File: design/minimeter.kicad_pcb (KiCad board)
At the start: 2 copper layers, 44.4 x 26.7 mm, 15 parts, among them J1 Conn_01x02_Pin, J2 I2C, SW1 SW_Push_Dual, SW2 SW_Push_Dual

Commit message: Implement negative voltage measurement
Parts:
- R2: value 10K -> 4.7K
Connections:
- net /PULL_10K renamed /PULL_4.7K
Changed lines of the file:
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@@
 	(net 11 "unconnected-(A1-RESET-PadRST2)")
 	(net 12 "/BTN_SEL")
-	(net 13 "/PULL_10K")
+	(net 13 "/PULL_4.7K")
 	(net 14 "unconnected-(A1-3.3V-Pad3V3)")
 	(net 15 "unconnected-(A1-PadD6)")
@@
 			)
 		)
-		(property "Value" "10K"
+		(property "Value" "4.7K"
 			(at 3.81 -2.37 0)
 			(layer "B.Fab")
@@
 			(layers "*.Cu" "*.Mask")
 			(remove_unused_layers no)
-			(net 13 "/PULL_10K")
+			(net 13 "/PULL_4.7K")
 			(pintype "passive")
 		)
@@
 			(layers "*.Cu" "*.Mask")
 			(remove_unused_layers no)
-			(net 13 "/PULL_10K")
+			(net 13 "/PULL_4.7K")
 			(pinfunction "D9")
 			(pintype "bidirectional")

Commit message: Update hardware to v3
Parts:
- removed R5: 220, Resistor_THT:R_Axial_DIN0207_L6.3mm_D2.5mm_P7.62mm_Horizontal
- C1: footprint Capacitor_THT:C_Rect_L7.0mm_W2.0mm_P5.00mm -> Capacitor_THT:C_Disc_D3.4mm_W2.1mm_P2.50mm
- R4: value 220 -> 100
- moved R2 1.27 mm to (57.1, 53.3)
- moved R3 1.27 mm to (57.1, 55.9)
- moved R4 1.27 mm to (57.1, 58.4)
- moved C1 0.64 mm to (73.7, 57.8)
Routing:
- net /IN_PROT: track 20.3 -> 26.5 mm
- net Net-(C1-Pad2): track 4.27 -> 6.01 mm
- net /PULL_1K: track 12.3 -> 11.0 mm
- net /PULL_110: track 8.67 -> 7.40 mm
- net /PULL_4.7K: track 15.9 -> 14.6 mm
- net /SPKR: track 15.0 -> 15.9 mm
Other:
- board text added: "MiniMeter v3 2026-01-28 Jasmine Tai"
- board text removed: "MiniMeter v2 2026-01-21 Jasmine Tai"

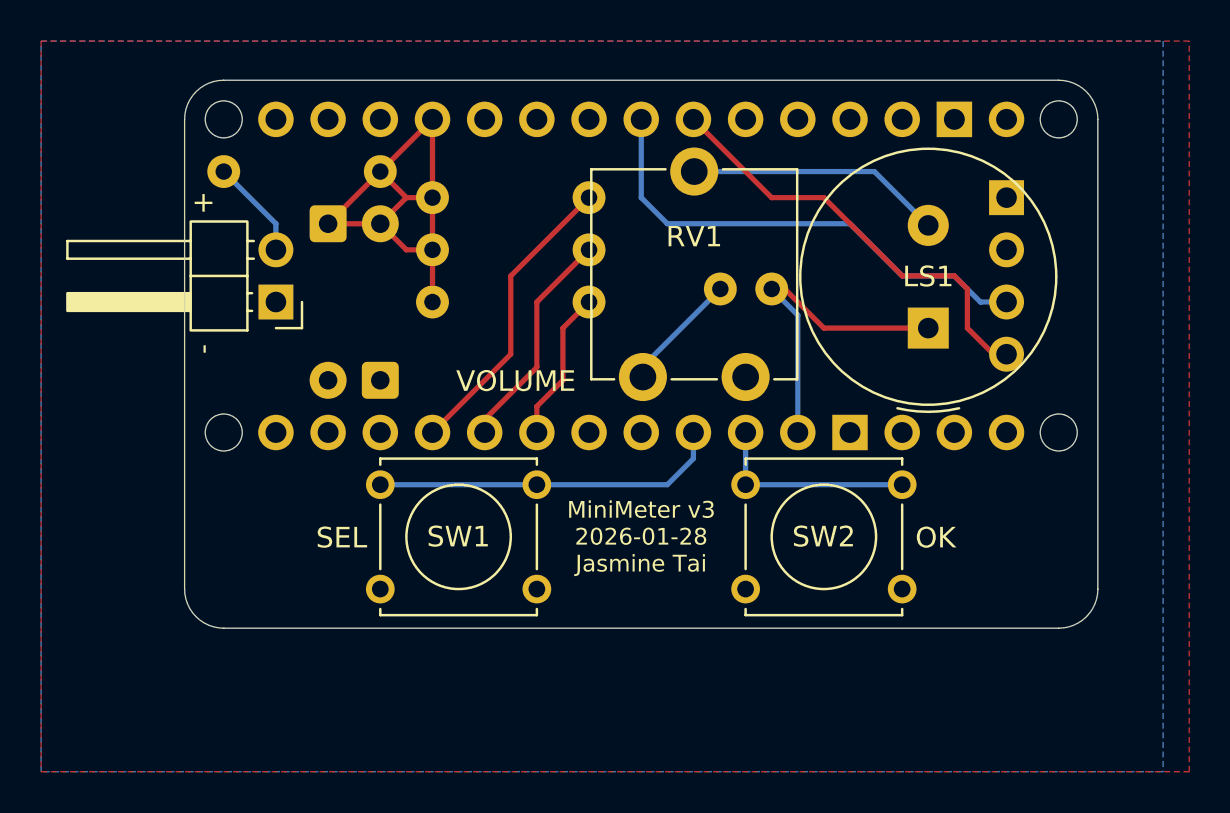
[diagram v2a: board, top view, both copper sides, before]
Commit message: Update footprints
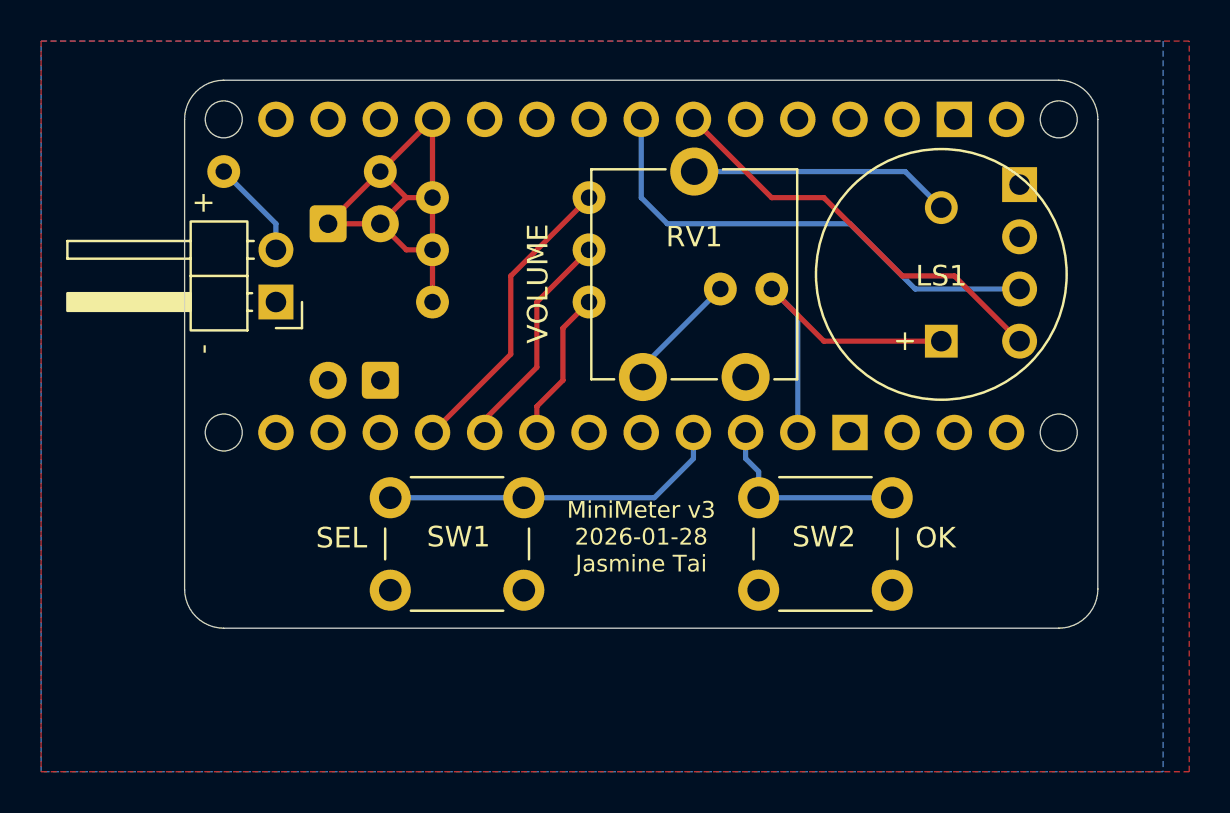
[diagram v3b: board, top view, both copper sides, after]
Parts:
- LS1: footprint Buzzer_Beeper:Buzzer_TDK_PS1240P02BT_D12.2mm_H6.5mm -> Buzzer_Beeper:MagneticBuzzer_ProSignal_ABT-410-RC
- SW1, SW2: footprint Button_Switch_THT:SW_Tactile_Straight_KSA0Axx1LFTR -> Button_Switch_THT:SW_PUSH_6mm
- moved LS1 0.90 mm to (81.9, 60.3)
- moved J2 0.90 mm to (85.7, 52.7)
- moved SW2 0.90 mm to (73.0, 67.9)
- moved SW1 0.80 mm to (55.1, 67.9)
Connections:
- net /PULL_110 renamed /PULL_100
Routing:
- net /SPKR: track 15.9 -> 16.8 mm
- net /SCL: track 21.1 -> 20.3 mm

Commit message: Update design to v4
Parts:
- added D3: LED_Filled, LED_THT:LED_D3.0mm, F.Cu at (49.5, 57.1)
- added R5: 820, Resistor_THT:R_Axial_DIN0207_L6.3mm_D2.5mm_P7.62mm_Horizontal, B.Cu at (47.0, 59.7)
- A1: footprint arduino-library:Arduino_Nano_Socket -> Module:Arduino_Nano_WithMountingHoles
- RV1: footprint Potentiometer_THT:Potentiometer_ACP_CA9-V10_Vertical -> Potentiometer_THT:Potentiometer_Bourns_3386F_Vertical
- moved A1 40.1 mm to (85.1, 64.8)
- moved D1 18.8 mm to (70.5, 52.1), turned to 180 degrees
- moved R1 11.4 mm to (52.1, 62.2), turned to 90 degrees
- moved J1 10.3 mm to (50.8, 68.6), turned to -90 degrees
- moved C1 4.62 mm to (74.9, 62.2)
- moved R4 4.58 mm to (59.7, 54.6), turned to -90 degrees
- moved SW1 3.90 mm to (59.0, 67.6)
- moved RV1 3.90 mm to (69.2, 59.8)
- moved R2 2.84 mm to (54.6, 54.6), turned to -90 degrees
- moved SW2 2.64 mm to (70.4, 67.6)
- moved D2 2.54 mm to (52.1, 52.1), turned to 0 degrees
- moved LS1 1.91 mm to (80.0, 60.3)
- moved R3 1.27 mm to (57.1, 54.6), turned to -90 degrees
- moved J2 0.90 mm to (85.1, 52.1)
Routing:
- net /IN_PROT: track 26.5 -> 0.00 mm
- net /PULL_4.7K: track 14.6 -> 3.59 mm
- net /SCL: track 20.3 -> 30.7 mm
- net /SPKR: track 16.8 -> 8.44 mm
- net /PULL_1K: track 11.0 -> 3.59 mm
- net Net-(D3-K): track 0.00 -> 6.13 mm
- net /LED: track 0.00 -> 5.08 mm
- net /BTN_SEL: track 16.8 -> 12.0 mm
- net /IN: track 4.86 -> 8.73 mm
- net /PULL_100: track 7.40 -> 3.59 mm
- net Net-(C1-Pad2): track 6.01 -> 9.28 mm
- net /SDA: track 24.1 -> 22.4 mm
- net Net-(LS1--): track 12.8 -> 13.7 mm
- added copper zone on B.Cu, net /IN_PROT
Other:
- board text added: "MiniMeter v4 2026.02.03 Jasmine Tai"
- board text removed: "MiniMeter v3 2026-01-28 Jasmine Tai"
- board text removed: "USB SIDE"

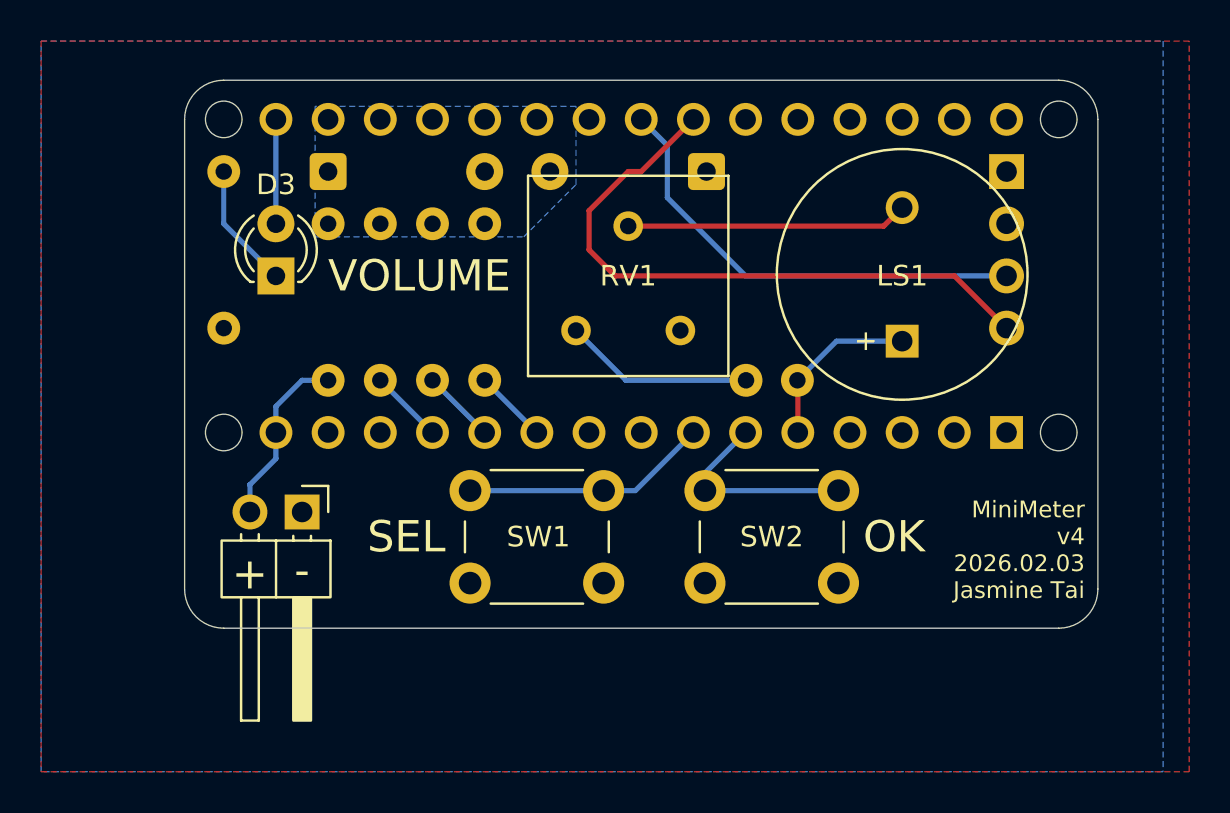
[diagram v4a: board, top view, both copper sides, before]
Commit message: Update PCB to v5 with updated trimpot footprint
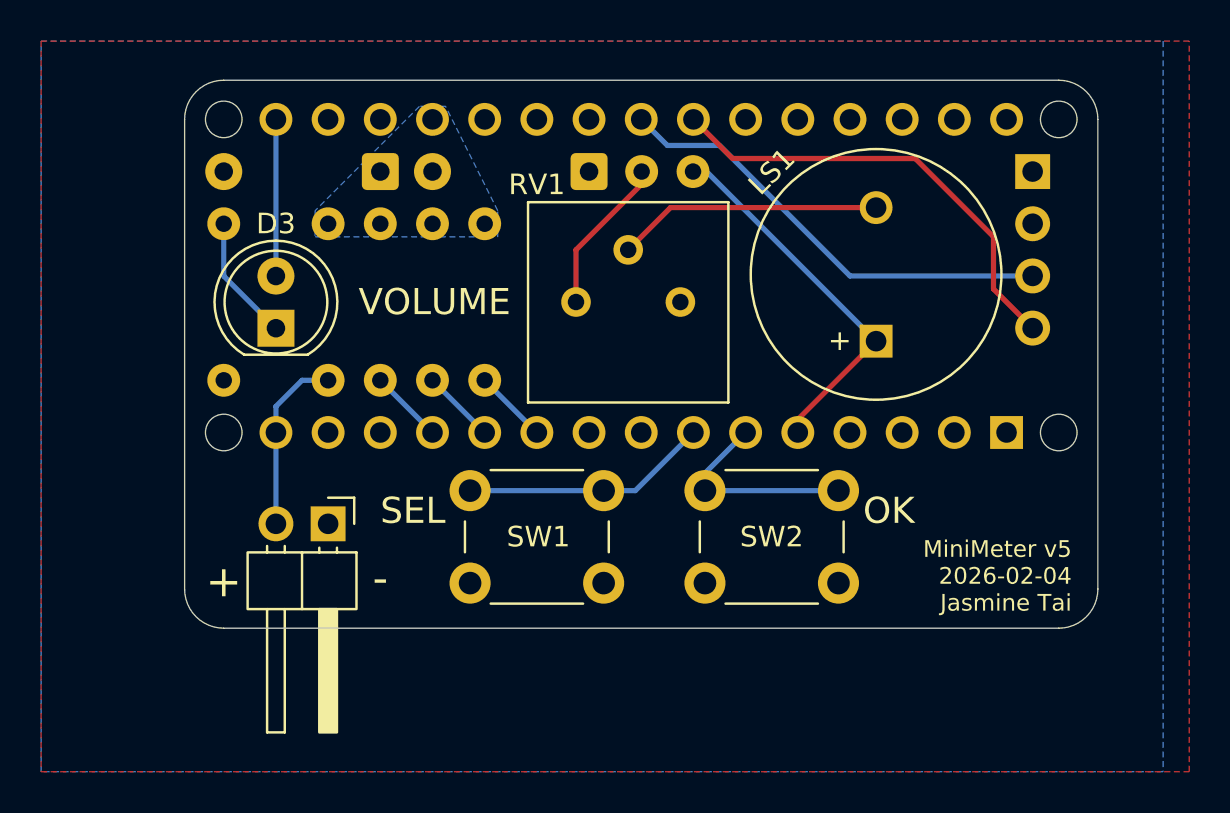
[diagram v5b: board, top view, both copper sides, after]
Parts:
- D3: footprint LED_THT:LED_D3.0mm -> LED_THT:LED_D5.0mm
- RV1: footprint Potentiometer_THT:Potentiometer_Bourns_3386F_Vertical -> Potentiometer_THT:Potentiometer_Bourns_3386P_Vertical
- moved C1 11.4 mm to (69.8, 52.1)
- moved D1 5.72 mm to (64.8, 52.1)
- moved D3 2.55 mm to (49.5, 59.7)
- moved D2 2.54 mm to (54.6, 52.1), turned to 180 degrees
- moved R5 2.54 mm to (47.0, 62.2)
- moved J1 1.39 mm to (52.1, 69.2)
- moved RV1 1.38 mm to (69.2, 58.4)
- moved LS1 1.27 mm to (78.7, 60.3)
- moved J2 1.27 mm to (86.4, 52.1)
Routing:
- net /SPKR: track 8.44 -> 18.4 mm
- net /SCL: track 30.7 -> 22.2 mm
- net /LED: track 5.08 -> 7.62 mm
- net Net-(C1-Pad2): track 9.28 -> 7.67 mm
- net Net-(LS1--): track 13.7 -> 12.9 mm
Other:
- board text added: "${TITLE} ${REVISION} ${ISSUE_DATE} ${COMPANY}"
- board text removed: "MiniMeter v4 2026.02.03 Jasmine Tai"

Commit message: Adjust PCB
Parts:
- moved J2 0.64 mm to (85.7, 52.1)
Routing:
- net /SCL: track 22.2 -> 20.8 mm
- net /SDA: track 22.2 -> 21.6 mm
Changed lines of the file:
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@@
 			(layer "B.Fab")
 		)
-		(fp_text user "USB"
-			(at 2.54 -35.56 0)
+		(fp_text user "USB Side"
+			(at -2.54 -35.56 0)
 			(unlocked yes)
 			(layer "B.SilkS")
@@
 	(footprint "Connector_PinSocket_2.54mm:PinSocket_1x04_P2.54mm_Horizontal"
 		(layer "B.Cu")
-		(at 86.36 52.07 180)
+		(at 85.725 52.07 180)
 		(descr "Through hole angled socket strip, 1x04, 2.54mm pitch, 8.51mm socket length, single row (from Kicad 4.0.7), script generated")
 		(tags "Through hole angled socket strip THT 1x04 2.54mm single row")
@@
 	)
 	(gr_text "Copyright\n© 2026\nJasmine Tai.\nAll rights\nreserved."
-		(at 87.63 69.85 0)
+		(at 88.265 70.485 0)
 		(layer "B.SilkS")
 		(effects
@@
 	)
 	(segment
-		(start 68.58 50.8)
-		(end 71.12 50.8)
+		(start 77.47 57.15)
+		(end 85.725 57.15)
 		(width 0.254)
 		(layer "B.Cu")
@@
 	)
 	(segment
-		(start 77.47 57.15)
-		(end 86.36 57.15)
-		(width 0.254)
-		(layer "B.Cu")
-		(net 3)
-	)
-	(segment
 		(start 67.31 49.53)
 		(end 68.58 50.8)
@@
 	)
 	(segment
-		(start 86.36 59.69)
-		(end 84.455 57.785)
+		(start 68.58 50.8)
+		(end 71.12 50.8)
 		(width 0.254)
-		(layer "F.Cu")
-		(net 4)
-	)
-	(segment
-		(start 80.645 51.435)
-		(end 71.755 51.435)
-		(width 0.254)
-		(layer "F.Cu")
-		(net 4)
-	)
-	(segment
-		(start 84.455 57.785)
-		(end 84.455 55.245)
-		(width 0.254)
-		(layer "F.Cu")
-		(net 4)
+		(layer "B.Cu")
+		(net 3)
 	)
 	(segment
@@
 	)
 	(segment
-		(start 84.455 55.245)
-		(end 80.645 51.435)
+		(start 83.82 56.515)
+		(end 78.74 51.435)
 		(width 0.254)
 		(layer "F.Cu")
+		(net 4)
+	)
+	(segment
+		(start 78.74 51.435)
+		(end 71.755 51.435)
+		(width 0.254)
+		(layer "F.Cu")
+		(net 4)
+	)
+	(segment
+		(start 83.82 57.785)
+		(end 83.82 56.515)
+		(width 0.254)
+		(layer "F.Cu")
+		(net 4)
+	)
+	(segment
+		(start 85.725 59.69)
+		(end 83.82 57.785)
+		(width 0.254)
+		(layer "F.Cu")
